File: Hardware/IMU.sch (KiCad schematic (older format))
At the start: 1 part

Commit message: Schematic and readme updated
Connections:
- net FSYNC: now also U?.11 (FSYNC)
- net INT: now also U?.12 (INT)
- net SCL: now also U?.9 (AD0/MISO)
- net SDA: now also U?.24 (SDA/MOSI)
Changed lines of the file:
@@
 	1    0    0    -1
 $EndComp
-Text HLabel 5050 3550 0    50   BiDi ~ 0
+Text HLabel 5150 3550 0    50   BiDi ~ 0
 SDA
-Text HLabel 5050 3650 0    50   Input ~ 0
+Text HLabel 5150 3650 0    50   Input ~ 0
 SCL
-Text HLabel 6450 3550 2    50   Output ~ 0
+Text HLabel 6350 3550 2    50   Output ~ 0
 INT
-Text HLabel 5050 4050 0    50   BiDi ~ 0
+Text HLabel 5150 4050 0    50   BiDi ~ 0
 FSYNC
 $EndSCHEMATC

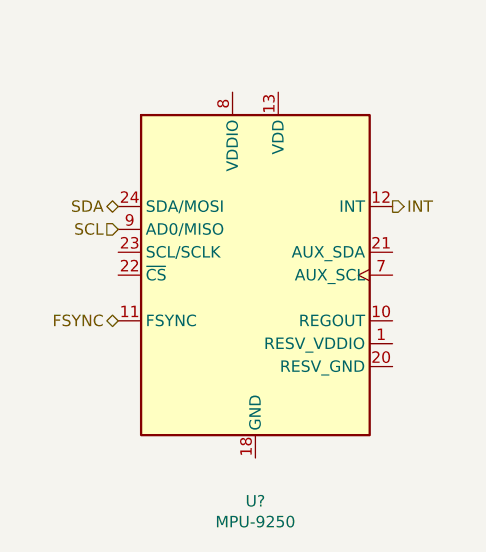
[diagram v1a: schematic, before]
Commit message: Battery charger IC added
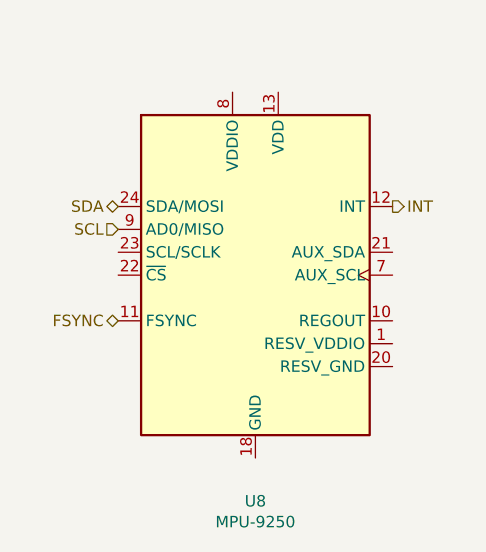
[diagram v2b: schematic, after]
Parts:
- gave numbers to parts that had none: 1
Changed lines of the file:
@@
 P 5750 3850
 AR Path="/5FF03C33" Ref="U?"  Part="1"
-AR Path="/5FF03301/5FF03C33" Ref="U?"  Part="1"
+AR Path="/5FF03301/5FF03C33" Ref="U8"  Part="1"
 AR Path="/5FF05F31/5FF03C33" Ref="U?"  Part="1"
-F 0 "U?" H 5750 2861 50  0000 C CNN
+F 0 "U8" H 5750 2861 50  0000 C CNN
 F 1 "MPU-9250" H 5750 2770 50  0000 C CNN
 F 2 "Sensor_Motion:InvenSense_QFN-24_3x3mm_P0.4mm" H 5750 2850 50  0001 C CNN

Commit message: Replaced ESP-WROOM-32D with ESP32-CAM
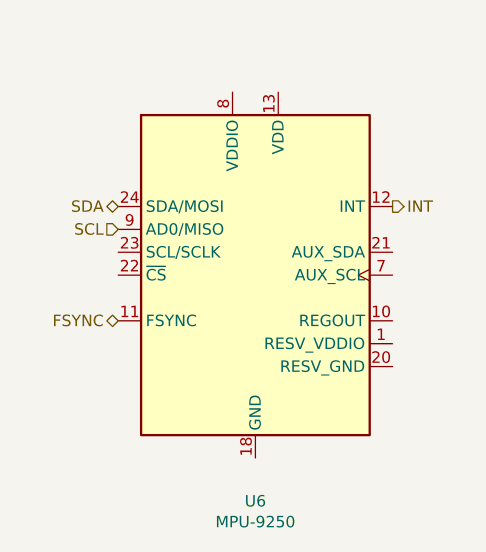
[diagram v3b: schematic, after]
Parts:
- renumbered U8 to U6
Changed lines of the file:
@@
 P 5750 3850
 AR Path="/5FF03C33" Ref="U?"  Part="1"
-AR Path="/5FF03301/5FF03C33" Ref="U8"  Part="1"
+AR Path="/5FF03301/5FF03C33" Ref="U6"  Part="1"
 AR Path="/5FF05F31/5FF03C33" Ref="U?"  Part="1"
-F 0 "U8" H 5750 2861 50  0000 C CNN
+F 0 "U6" H 5750 2861 50  0000 C CNN
 F 1 "MPU-9250" H 5750 2770 50  0000 C CNN
 F 2 "Sensor_Motion:InvenSense_QFN-24_3x3mm_P0.4mm" H 5750 2850 50  0001 C CNN

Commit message: Signed-off-by: Usman <usmanmehmood55@gmail.com>
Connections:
- net +3V3: now reaches U6.13 (VDD)
- net +3V3: now also U6.8 (VDDIO)
- net GND: now reaches U6.18 (GND)
- no-connect marks 0 -> 7
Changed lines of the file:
@@
 AR Path="/5FF03301/5FF03C33" Ref="U6"  Part="1"
 AR Path="/5FF05F31/5FF03C33" Ref="U?"  Part="1"
-F 0 "U6" H 5750 2861 50  0000 C CNN
-F 1 "MPU-9250" H 5750 2770 50  0000 C CNN
+F 0 "U6" H 6200 4750 50  0000 C CNN
+F 1 "MPU-9250" H 6200 4650 50  0000 C CNN
 F 2 "Sensor_Motion:InvenSense_QFN-24_3x3mm_P0.4mm" H 5750 2850 50  0001 C CNN
 F 3 "https://store.invensense.com/datasheets/invensense/MPU9250REV1.0.pdf" H 5750 3700 50  0001 C CNN
@@
 Text HLabel 5150 4050 0    50   BiDi ~ 0
 FSYNC
+NoConn ~ 5150 3750
+NoConn ~ 5150 3850
+NoConn ~ 6350 3750
+NoConn ~ 6350 3850
+NoConn ~ 6350 4050
+NoConn ~ 6350 4150
+NoConn ~ 6350 4250
+$Comp
+L power:+3.3V #PWR0101
+U 1 1 6070917E
+P 5750 2950
+F 0 "#PWR0101" H 5750 2800 50  0001 C CNN
+F 1 "+3.3V" H 5765 3123 50  0000 C CNN
+F 2 "" H 5750 2950 50  0001 C CNN
+F 3 "" H 5750 2950 50  0001 C CNN
+	1    5750 2950
+	1    0    0    -1
+$EndComp
+Wire Wire Line
+	5750 2950 5750 3000
+Wire Wire Line
+	5750 3000 5650 3000
+Wire Wire Line
+	5650 3000 5650 3050
+Wire Wire Line
+	5750 3000 5850 3000
+Wire Wire Line
+	5850 3000 5850 3050
+Connection ~ 5750 3000
+$Comp
+L power:GND #PWR0102
+U 1 1 60709BC2
+P 5750 4650
+F 0 "#PWR0102" H 5750 4400 50  0001 C CNN
+F 1 "GND" H 5755 4477 50  0000 C CNN
+F 2 "" H 5750 4650 50  0001 C CNN
+F 3 "" H 5750 4650 50  0001 C CNN
+	1    5750 4650
+	1    0    0    -1
+$EndComp
 $EndSCHEMATC

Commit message: Schematic updated, USB comms circuit added
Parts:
- renumbered U6 to U7
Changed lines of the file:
@@
 $Descr A4 11693 8268
 encoding utf-8
-Sheet 7 9
+Sheet 7 11
 Title ""
 Date ""
@@
 P 5750 3850
 AR Path="/5FF03C33" Ref="U?"  Part="1"
-AR Path="/5FF03301/5FF03C33" Ref="U6"  Part="1"
+AR Path="/5FF03301/5FF03C33" Ref="U7"  Part="1"
 AR Path="/5FF05F31/5FF03C33" Ref="U?"  Part="1"
-F 0 "U6" H 6200 4750 50  0000 C CNN
+F 0 "U7" H 6200 4750 50  0000 C CNN
 F 1 "MPU-9250" H 6200 4650 50  0000 C CNN
 F 2 "Sensor_Motion:InvenSense_QFN-24_3x3mm_P0.4mm" H 5750 2850 50  0001 C CNN
@@
 NoConn ~ 6350 4250
 $Comp
-L power:+3.3V #PWR0101
+L power:+3.3V #PWR049
 U 1 1 6070917E
 P 5750 2950
-F 0 "#PWR0101" H 5750 2800 50  0001 C CNN
+F 0 "#PWR049" H 5750 2800 50  0001 C CNN
 F 1 "+3.3V" H 5765 3123 50  0000 C CNN
 F 2 "" H 5750 2950 50  0001 C CNN
@@
 Connection ~ 5750 3000
 $Comp
-L power:GND #PWR0102
+L power:GND #PWR050
 U 1 1 60709BC2
 P 5750 4650
-F 0 "#PWR0102" H 5750 4400 50  0001 C CNN
+F 0 "#PWR050" H 5750 4400 50  0001 C CNN
 F 1 "GND" H 5755 4477 50  0000 C CNN
 F 2 "" H 5750 4650 50  0001 C CNN

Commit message: PCB design started
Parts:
- U7: symbol Sensor_Motion:MPU-9250 -> Roverette-rescue:MPU-9250-Sensor_Motion
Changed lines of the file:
@@
 $EndDescr
 $Comp
-L Sensor_Motion:MPU-9250 U?
+L Roverette-rescue:MPU-9250-Sensor_Motion U?
 U 1 1 5FF03C33
 P 5750 3850
@@
 NoConn ~ 6350 4250
 $Comp
-L power:+3.3V #PWR049
+L Roverette-rescue:+3.3V-power #PWR049
 U 1 1 6070917E
 P 5750 2950
@@
 Connection ~ 5750 3000
 $Comp
-L power:GND #PWR050
+L Roverette-rescue:GND-power #PWR050
 U 1 1 60709BC2
 P 5750 4650
